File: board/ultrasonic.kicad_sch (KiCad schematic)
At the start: 34 parts, among them J4 SWIM, U8 STM8S003F3P, U9 MAX202

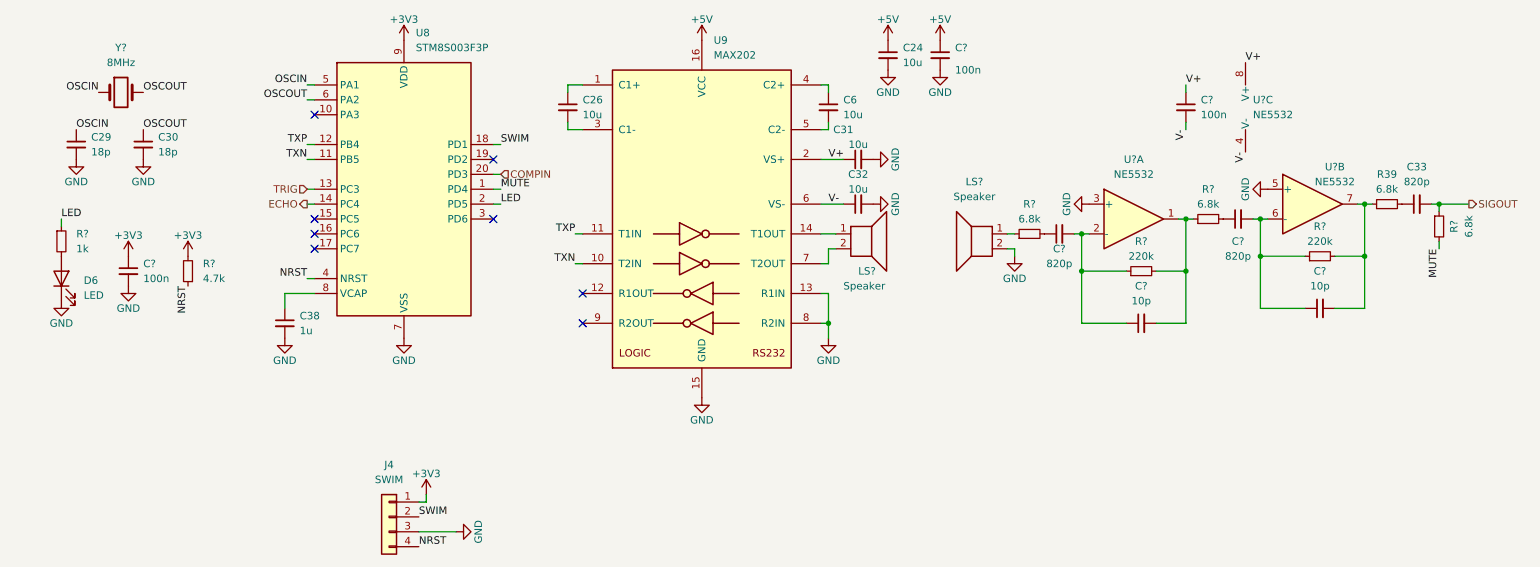
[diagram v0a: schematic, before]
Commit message: First placement of parts, fixed a few bugs in the schematic
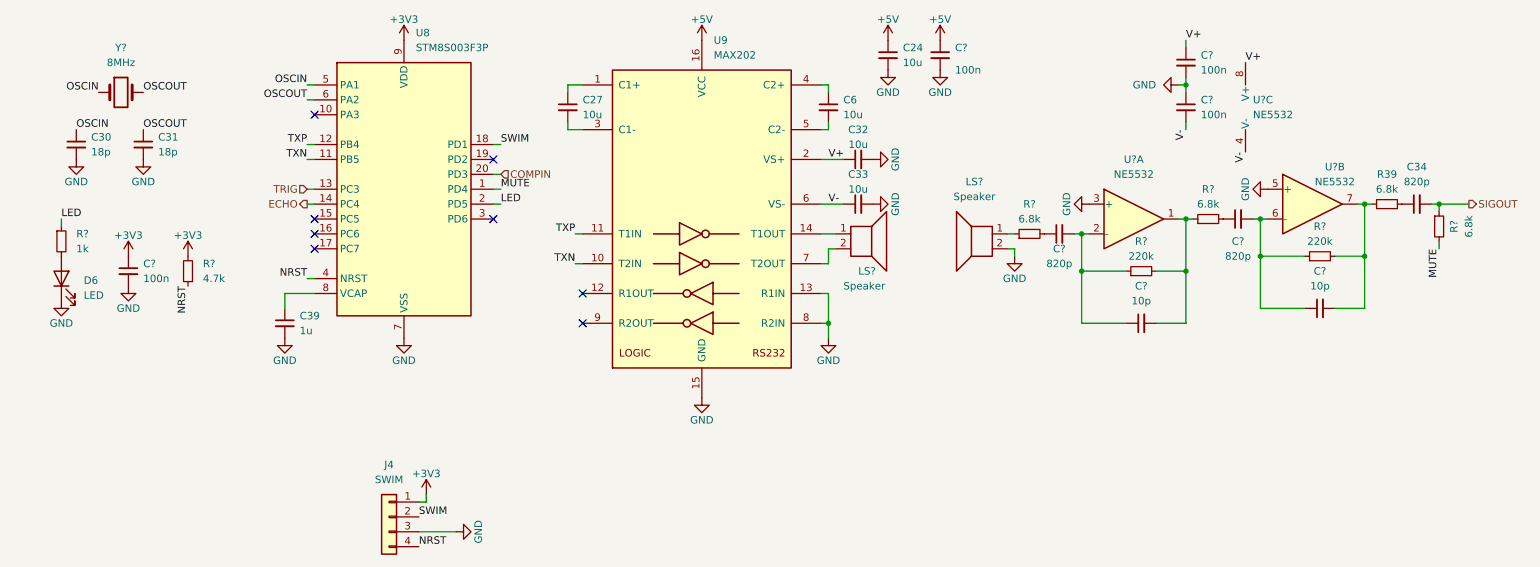
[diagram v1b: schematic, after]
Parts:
- added C?: 100n, Capacitor_SMD:C_0603_1608Metric_Pad1.08x0.95mm_HandSolder, symbol Device:C_Small
- renumbered C26 to C27, C29 to C30, C30 to C31, C31 to C32, C32 to C33, C33 to C34, C38 to C39
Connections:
- net GND: now also C?.1, C?.2
- net V+: now also C?.1; no longer C?.1

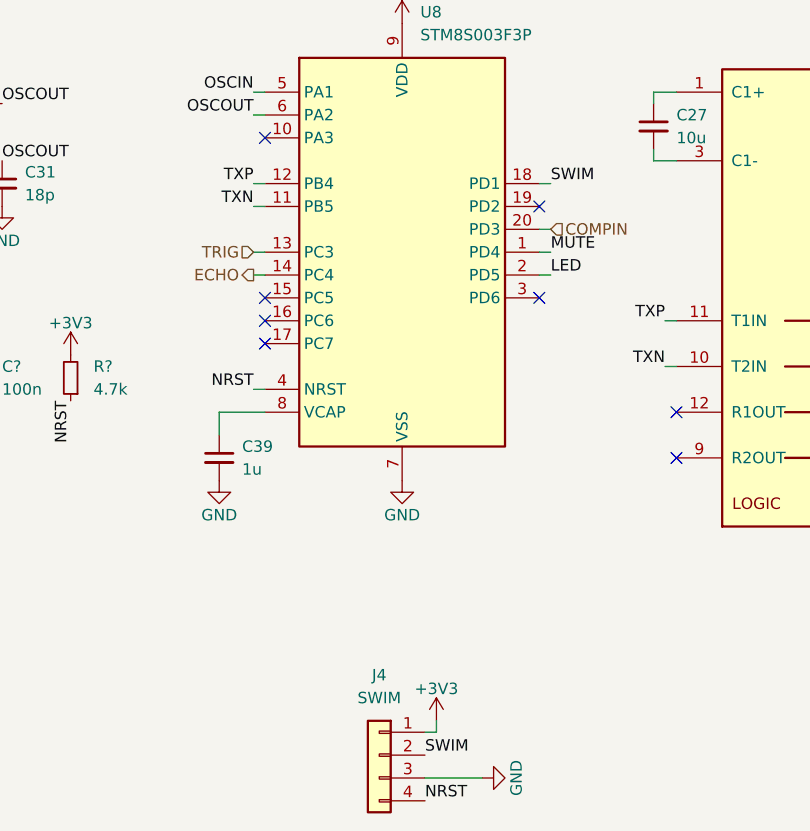
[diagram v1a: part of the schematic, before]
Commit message: Replaced the component groups to get a tighter fit and routed most of the ultrasonic sensors
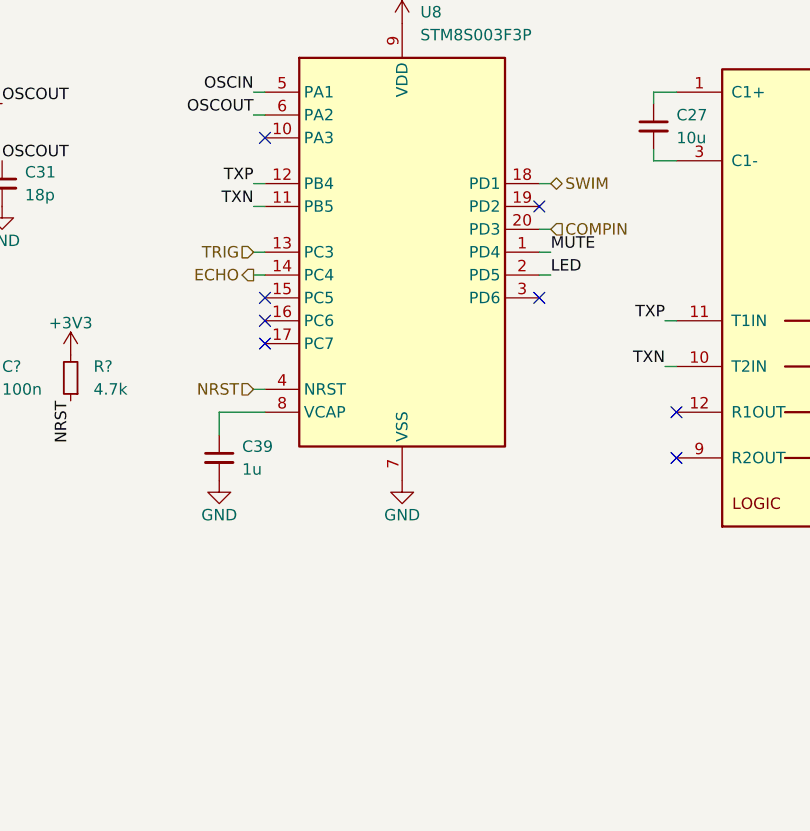
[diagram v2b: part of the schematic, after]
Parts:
- removed J4: SWIM, Connector_PinHeader_2.54mm:PinHeader_1x04_P2.54mm_Vertical, symbol Connector_Generic:Conn_01x04

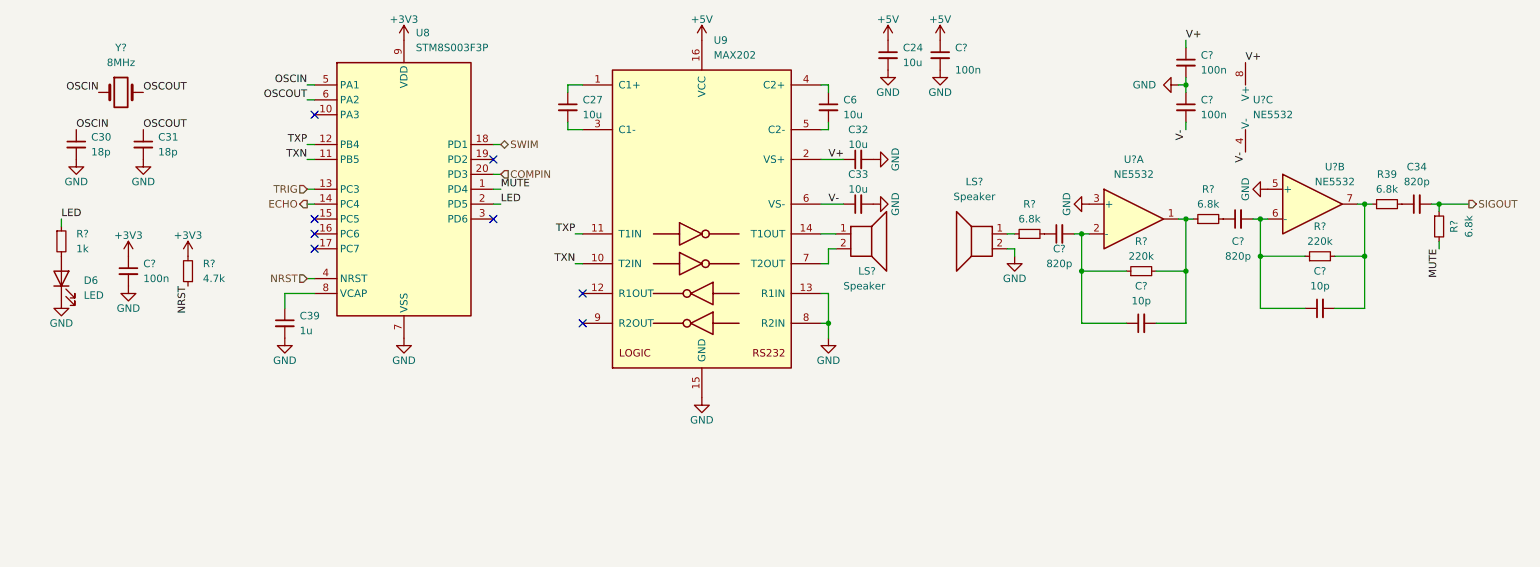
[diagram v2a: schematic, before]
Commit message: Everything routed, a few changes in the components, first prototypes ordered
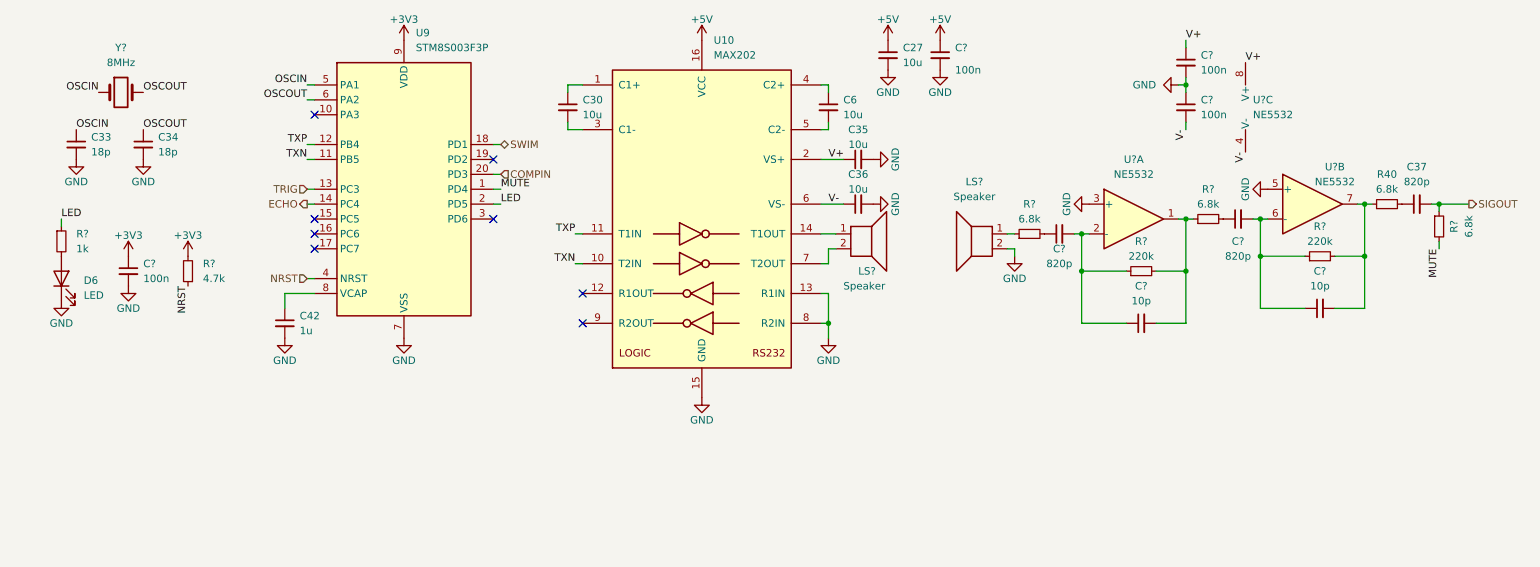
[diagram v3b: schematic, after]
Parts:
- D6: footprint LED_SMD:LED_0603_1608Metric_Pad1.05x0.95mm_HandSolder -> LED_SMD:LED_0603_1608Metric; JLC_PN C2286 -> C72043; MPN KT-0603R -> 19-217/GHC-YR1S2/3T; Manufacturer Hubei KENTO Elec -> Everlight Elec
- R40: renamed from R39; JLC_BasicPart (none) -> yes
- R? (x5): JLC_BasicPart (none) -> yes
- renumbered C24 to C27, C27 to C30, C30 to C33, C31 to C34, C32 to C35, C33 to C36, C34 to C37, C39 to C42, U9 to U10, U8 to U9

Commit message: Updated price information for 10x and added a calculation for 20 boards including all parts and assembly cost
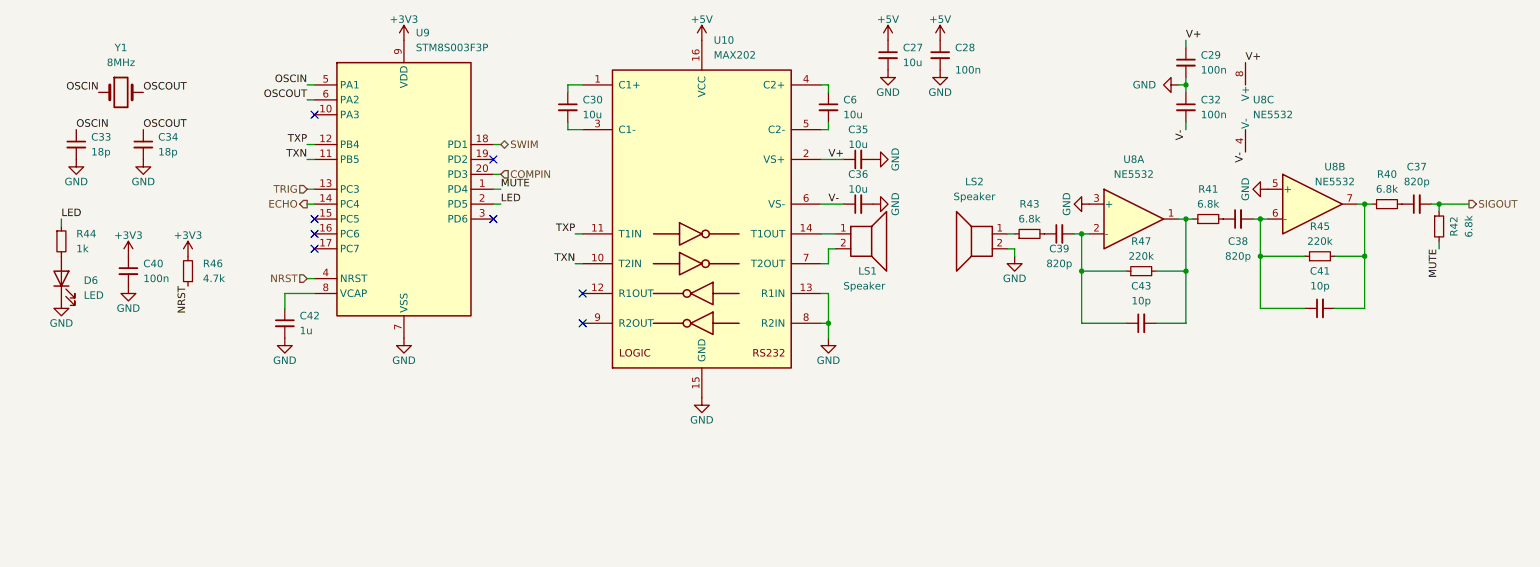
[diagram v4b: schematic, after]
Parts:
- C27, C30, C35, C36, C6: JLC_Price10 (none) -> 0.0237
- C28, C29, C32, C40: renamed from C?; JLC_Price10 0.0042 -> 0.0021
- C33, C34: JLC_Price10 (none) -> 0.0064
- C37: JLC_Price10 (none) -> 0.0038
- C38, C39: renamed from C?; JLC_Price10 (none) -> 0.0038
- C41, C43: renamed from C?; JLC_Price10 (none) -> 0.0054
- C42: JLC_Price10 (none) -> 0.0051
- D6: JLC_Price10 0.0106 -> 0.0248
- LS1, LS2: renamed from LS?; JLC_Price10 (none) -> 1.2985
- R40: JLC_Price10 (none) -> 0.0009
- R41, R42, R43, R45, R47: renamed from R?; JLC_Price10 (none) -> 0.0009
- R44: renamed from R?; JLC_Price10 (none) -> 0.0005
- R46: renamed from R?; JLC_Price10 (none) -> 0.001
- U10: JLC_Price10 (none) -> 1.1165
- U8: renamed from U?; JLC_Price10 (none) -> 0.2156
- U9: JLC_Price10 (none) -> 0.3668
- Y1: renamed from Y?; JLC_Price10 (none) -> 0.1689

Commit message: Updated schematic to new revision: Switch ultrasonic modules to PGA460, using ublox M10 GPS
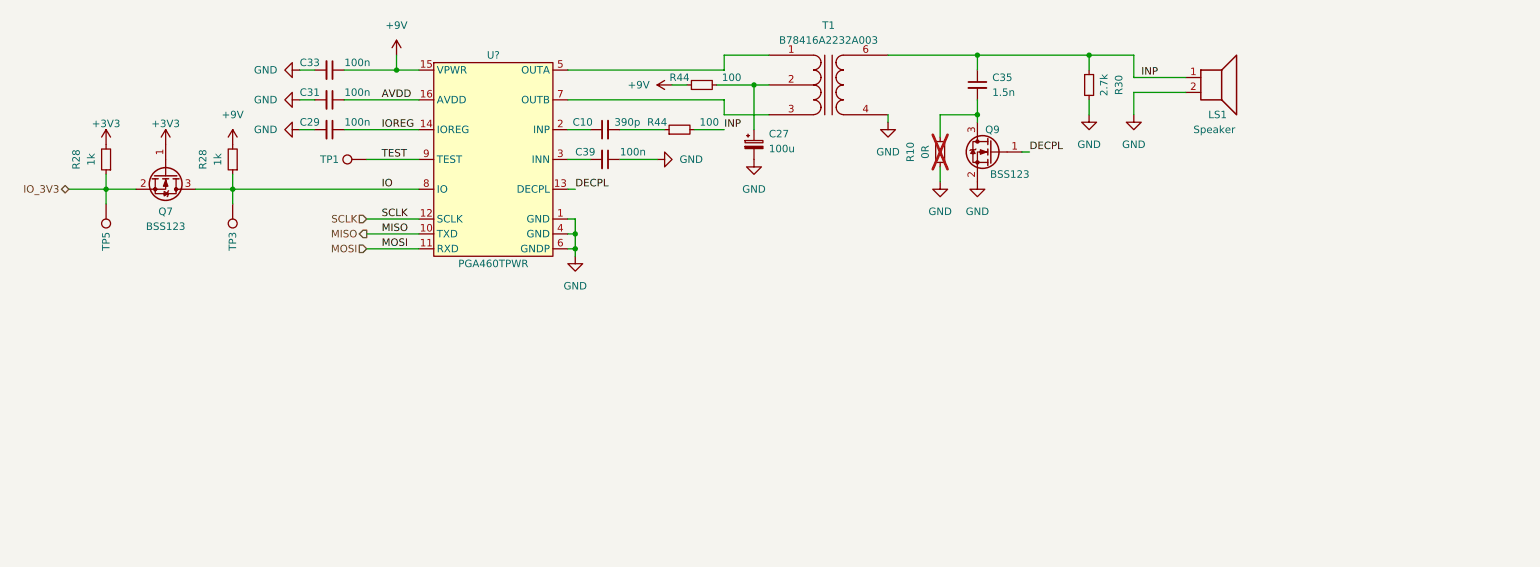
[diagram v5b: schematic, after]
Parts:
- removed C27, C30, C36: 10u, Capacitor_SMD:C_1206_3216Metric_Pad1.33x1.80mm_HandSolder, symbol Device:C_Small
- removed C28, C32, C40: 100n, Capacitor_SMD:C_0603_1608Metric_Pad1.08x0.95mm_HandSolder, symbol Device:C_Small
- removed C34: 18p, Capacitor_SMD:C_0603_1608Metric_Pad1.08x0.95mm_HandSolder, symbol Device:C_Small
- removed C37: 820p, Capacitor_SMD:C_0603_1608Metric_Pad1.08x0.95mm_HandSolder, symbol Device:C_Small
- removed C38: 1n, Capacitor_SMD:C_0603_1608Metric_Pad1.08x0.95mm_HandSolder, symbol Device:C_Small
- removed C41, C43: 22p, Capacitor_SMD:C_0603_1608Metric_Pad1.08x0.95mm_HandSolder, symbol Device:C_Small
- removed C42: 1u, Capacitor_SMD:C_0603_1608Metric_Pad1.08x0.95mm_HandSolder, symbol Device:C_Small
- removed C6: 1u, Capacitor_SMD:C_1206_3216Metric_Pad1.33x1.80mm_HandSolder, symbol Device:C_Small
- removed D6: LED, LED_SMD:LED_0603_1608Metric, symbol Device:LED
- removed LS2: Speaker, Capacitor_THT:CP_Radial_D10.0mm_P5.00mm, symbol Device:Speaker
- removed R40, R41, R43: 6.8k, Resistor_SMD:R_0603_1608Metric, symbol Device:R_Small
- removed R42, R45, R47: 75k, Resistor_SMD:R_0603_1608Metric, symbol Device:R_Small
- removed R44: 1k, Resistor_SMD:R_0603_1608Metric, symbol Device:R_Small
- removed R46: 4.7k, Resistor_SMD:R_0603_1608Metric, symbol Device:R_Small
- removed U10: MAX202, Package_SO:SO-16_3.9x9.9mm_P1.27mm, symbol Interface_UART:MAX202
- removed U8: NE5532, Package_SO:SOIC-8_3.9x4.9mm_P1.27mm, symbol Amplifier_Operational:NE5532
- removed U9: STM8S003F3P, Package_SO:TSSOP-20_4.4x6.5mm_P0.65mm, symbol MCU_ST_STM8:STM8S003F3P
- removed Y1: Crystal, Crystal:Crystal_SMD_5032-2Pin_5.0x3.2mm_HandSoldering, symbol Device:Crystal
- added C10: 390p, Capacitor_SMD:C_0603_1608Metric, symbol Device:C_Small
- added C27: 100u, Capacitor_SMD:CP_Elec_6.3x5.2, symbol Device:C_Polarized_Small
- added C31: 100n, Capacitor_SMD:C_0603_1608Metric, symbol Device:C_Small
- added Q7, Q9: BSS123, Package_TO_SOT_SMD:SOT-23, symbol Transistor_FET:BSS123
- added R10: 0R, Resistor_SMD:R_0603_1608Metric, symbol Device:R_Small
- added R28 (x2): 1k, Resistor_SMD:R_0603_1608Metric, symbol Device:R_Small
- added R30: 2.7k, Resistor_SMD:R_0603_1608Metric, symbol Device:R_Small
- added R44 (x2): 100, Resistor_SMD:R_0603_1608Metric, symbol Device:R_Small
- added T1: B78416A2232A003, OBSPro:B78416AxA003, symbol OBSPro:B78416A2232A003
- added TP1, TP3, TP5: TestPoint, symbol Connector:TestPoint
- added U?: PGA460TPWR, OBSPro:TSSOP-14-1EP_2.6x2.6mm_P0.65mm, symbol OBSPro:PGA460
- C29: footprint Capacitor_SMD:C_0603_1608Metric_Pad1.08x0.95mm_HandSolder -> Capacitor_SMD:C_0603_1608Metric
- C33: value 18p -> 100n; footprint Capacitor_SMD:C_0603_1608Metric_Pad1.08x0.95mm_HandSolder -> Capacitor_SMD:C_0603_1608Metric; JLC_PN C1647 -> C14663; JLC_Price1 (none) -> 0.042; JLC_Price10 0.0064 -> 0.0021; JLC_Price100 (none) -> 0.0021; JLC_Price1000 (none) -> 0.0014; MPN CL10C180JB8NNNC -> CC0603KRX7R9BB104; Manufacturer Samsung Electro-Mechanics -> YAGEO; kicost:JLC:pricing 1: USD 0.0069; 200: USD 0.0058; 800: USD 0.0051; 1600: USD 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 -> 1: USD 0.0020; 200: USD 0.0016; 800: USD 0.0013; 1600: USD 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
- C35: value 10u -> 1.5n; footprint Capacitor_SMD:C_1206_3216Metric_Pad1.33x1.80mm_HandSolder -> Capacitor_SMD:C_0603_1608Metric; JLC_BasicPart yes -> no; JLC_PN C13585 -> C96090; JLC_Price10 0.0237 -> (none); MPN CL31A106KBHNNNE -> CC0603KRX7R9BB152; Manufacturer Samsung Electro-Mechanics -> YAGEO
- C39: value 10n -> 100n; footprint Capacitor_SMD:C_0603_1608Metric_Pad1.08x0.95mm_HandSolder -> Capacitor_SMD:C_0603_1608Metric; JLC_BasicPart no -> yes; JLC_PN C107057 -> C14663; JLC_Price1 (none) -> 0.042; JLC_Price10 0.0038 -> 0.0021; JLC_Price100 (none) -> 0.0021; JLC_Price1000 (none) -> 0.0014; MPN CC0603JRNPO9BN821 -> CC0603KRX7R9BB104; PCBA (none) -> yes; kicost:JLC:pricing (none) -> 1: USD 0.0020; 200: USD 0.0016; 800: USD 0.0013; 1600: USD 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
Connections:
- net +3V3: now also Q7.1 (G), R28.2
- net GND: now also C39.1, LS1.2, C27.2, C31.2, Q9.2 (S), R10.1, R30.2, T1.4 (S1), U?.1 (GND), U?.4 (GND), U?.6 (GNDP); no longer C35.2
- net at C39.2: now also U?.3 (INN)
- net INP: now reaches LS1.1
- net INP: now also C35.1, R30.1, R44.2, T1.6 (S2)
- net OSCIN renamed +9V
- net +9V: now also R28.2, R44.1, U?.15 (VPWR)
- net V+ renamed IOREG
- net IOREG: now also U?.14 (IOREG); no longer C35.1
- new net: C35.2, Q9.3 (D), R10.2
- new net: C27.1, R44.2, T1.2 (PM)
- new net: C10.1, U?.2 (INP)
- new net: C10.2, R44.1
- new net: T1.1 (PR1), U?.5 (OUTA)
- new net: T1.3 (PR2), U?.7 (OUTB)
- new net AVDD: C31.1, U?.16 (AVDD)
- new net DECPL: Q9.1 (G), U?.13 (DECPL)
- new net IO: Q7.3 (D), R28.1, TP3.1, U?.8 (IO)
- new net IO_3V3: Q7.2 (S), R28.1, TP5.1
- new net MISO: U?.10 (TXD)
- new net MOSI: U?.11 (RXD)
- new net SCLK: U?.12 (SCLK)
- new net TEST: TP1.1, U?.9 (TEST)
- no-connect marks 8 -> 0
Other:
- moved on the sheet: LS1

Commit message: Fixed ERC errors
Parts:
- TP2: renamed from TP1; footprint (none) -> TestPoint:TestPoint_Pad_1.0x1.0mm
- TP3: renamed from TP5; footprint (none) -> TestPoint:TestPoint_Pad_1.0x1.0mm
- TP4: renamed from TP3; footprint (none) -> TestPoint:TestPoint_Pad_1.0x1.0mm
- U8: renamed from U?; footprint OBSPro:TSSOP-14-1EP_2.6x2.6mm_P0.65mm -> Package_SO:TSSOP-16_4.4x5mm_P0.65mm
- renumbered C33 to C34, C31 to C36, C29 to C37, C27 to C39, C39 to C40, Q9 to Q7, Q7 to Q8
